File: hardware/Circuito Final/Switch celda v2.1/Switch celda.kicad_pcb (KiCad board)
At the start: 2 copper layers, 98.6 x 38 mm, 34 parts, among them Q1 MMBT2222A, Q2 MMBT2907A, Q3 MMBT2222A

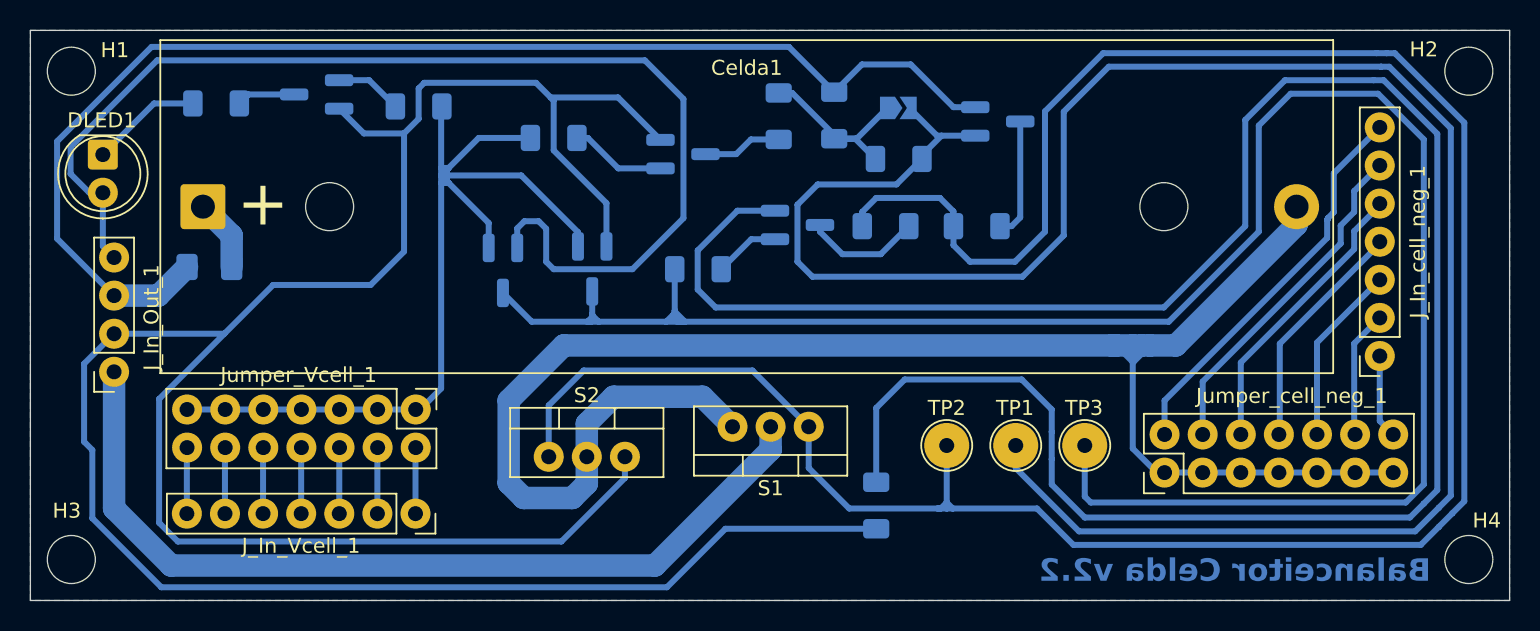
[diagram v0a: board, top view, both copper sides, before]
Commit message: subida de imágenes de cell_neg negativo y celdas v2.1 y v2.2 con los modelos 3D corregidos
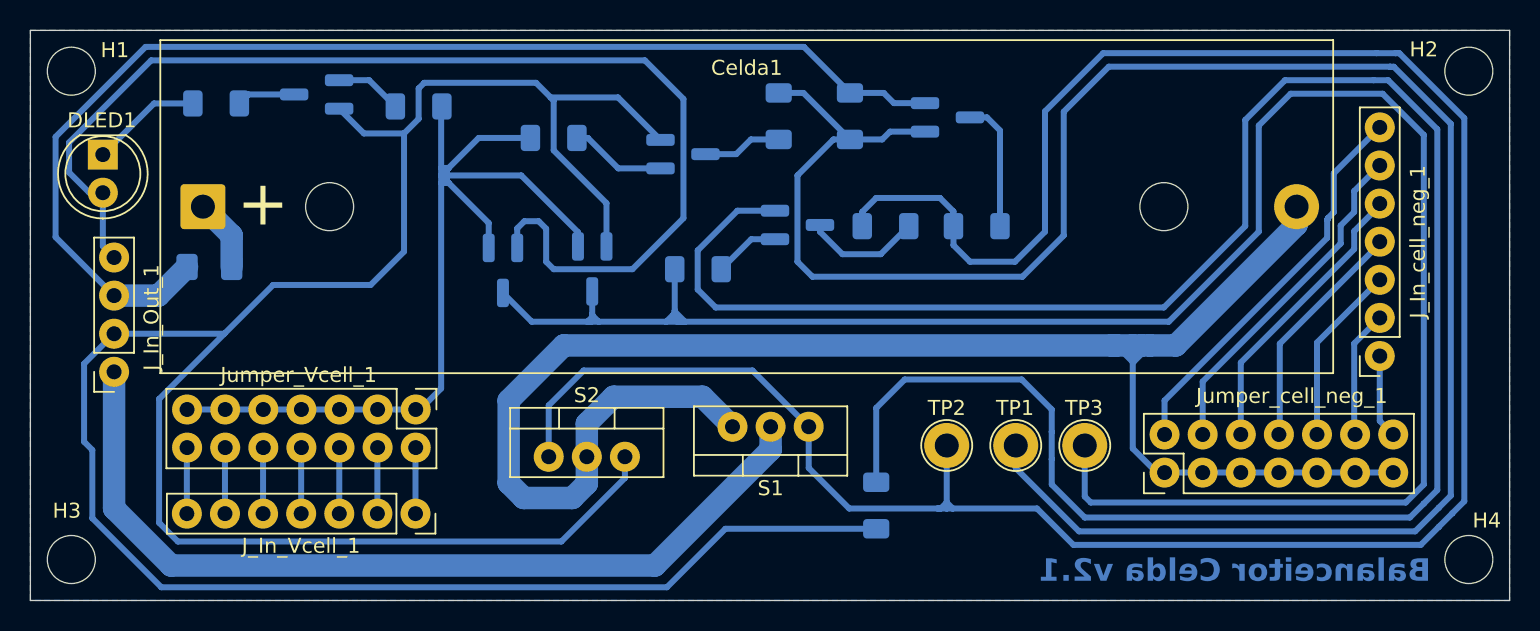
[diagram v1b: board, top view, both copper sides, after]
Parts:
- removed JP1: SolderJumper1, Jumper:SolderJumper-2_P1.3mm_Open_TrianglePad1.0x1.5mm
- removed R10: TBD, Resistor_SMD:R_1206_3216Metric_Pad1.30x1.75mm_HandSolder
- moved Q2 3.36 mm to (161.2, 90.1)
- moved R2 1.05 mm to (154.8, 90.0)
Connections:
- Q2 pad 2: Net-(JP1-B) -> Net-(Q2-B)
- R2 pad 1: Net-(JP1-A) -> Net-(Q2-B)
- R3 pad 2: Net-(JP1-A) -> Net-(Q2-B)
- TP1 pad 1: Net-(JP1-B) -> Net-(Q2-B)
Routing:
- net Net-(Q2-B): track 0.00 -> 135.7 mm
- net Net-(JP1-B): track 134.5 -> 0.00 mm
- net Net-(JP1-A): track 12.8 -> 0.00 mm
- net bus_pos: track 84.5 -> 80.3 mm
- net Net-(Q2-C): track 7.99 -> 8.74 mm
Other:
- board text added: "Balanceitor Celda v2.1"
- board text removed: "Balanceitor Celda v2.2"
